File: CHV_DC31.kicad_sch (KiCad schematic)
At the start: 84 parts, among them IC1 W25Q16JVUXIQ_TR, J1 USB_C_Receptacle_USB2.0, J2 Conn_01x02, J3 Conn_02x03_Odd_Even, J4 Conn_02x03_Odd_Even, J5 Conn_02x03_Odd_Even, J6 Conn_01x03, SW2 SW_SPST, SW3 SW_SPST, SW4 SW_SPST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

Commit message: updates
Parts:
- J2: footprint Connector_PinHeader_2.54mm:PinHeader_1x02_P2.54mm_Vertical -> Jumper:SolderJumper-2_P1.3mm_Open_Pad1.0x1.5mm
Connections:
- net RP1_CAN_RX: now also U3.5 (GPIO3); no longer U3.28 (GPIO17)
- net RP1_CAN_TX: now also U3.6 (GPIO4); no longer U3.27 (GPIO16)
- net RP1_LED_1: now also U3.15 (GPIO12); no longer U3.7 (GPIO5)
- net RP1_LED_2: now also U3.16 (GPIO13); no longer U3.8 (GPIO6)
- net RP1_LED_3: now also U3.12 (GPIO9); no longer U3.9 (GPIO7)

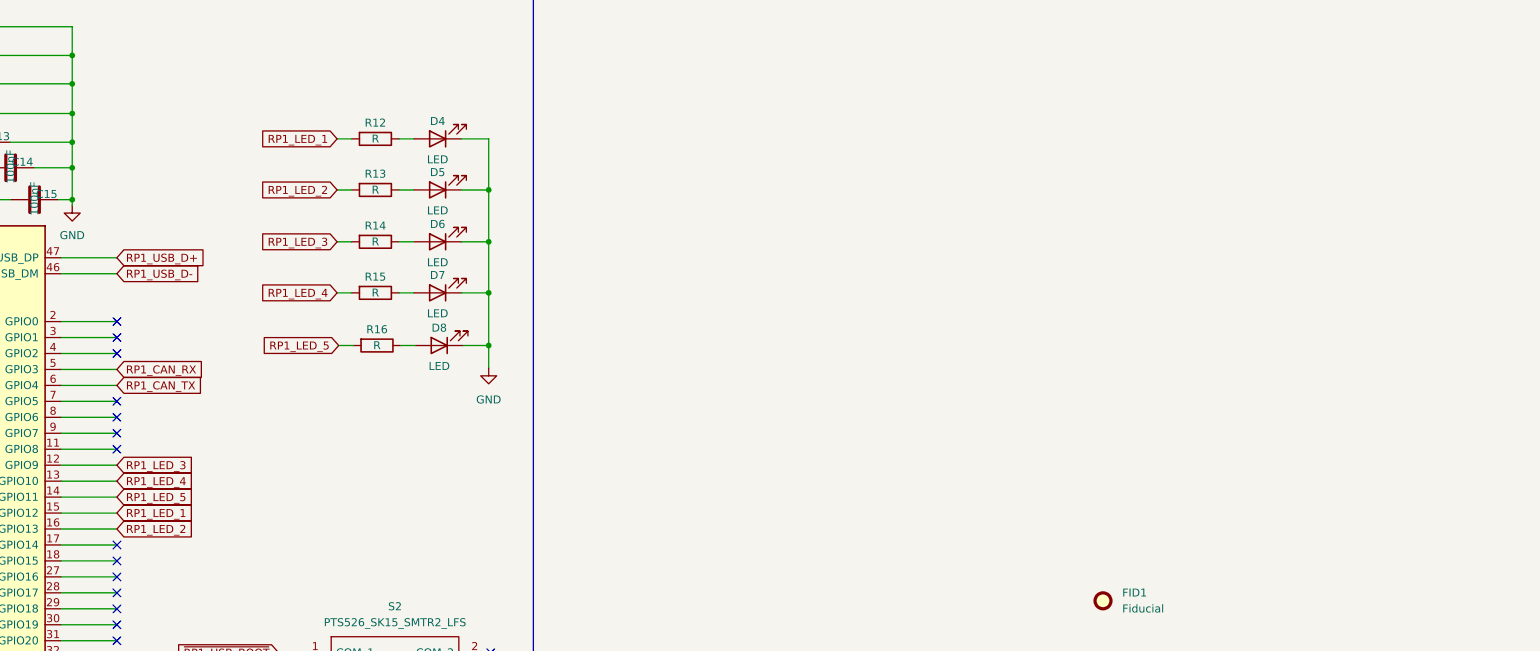
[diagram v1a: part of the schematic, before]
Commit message: layed out led ring
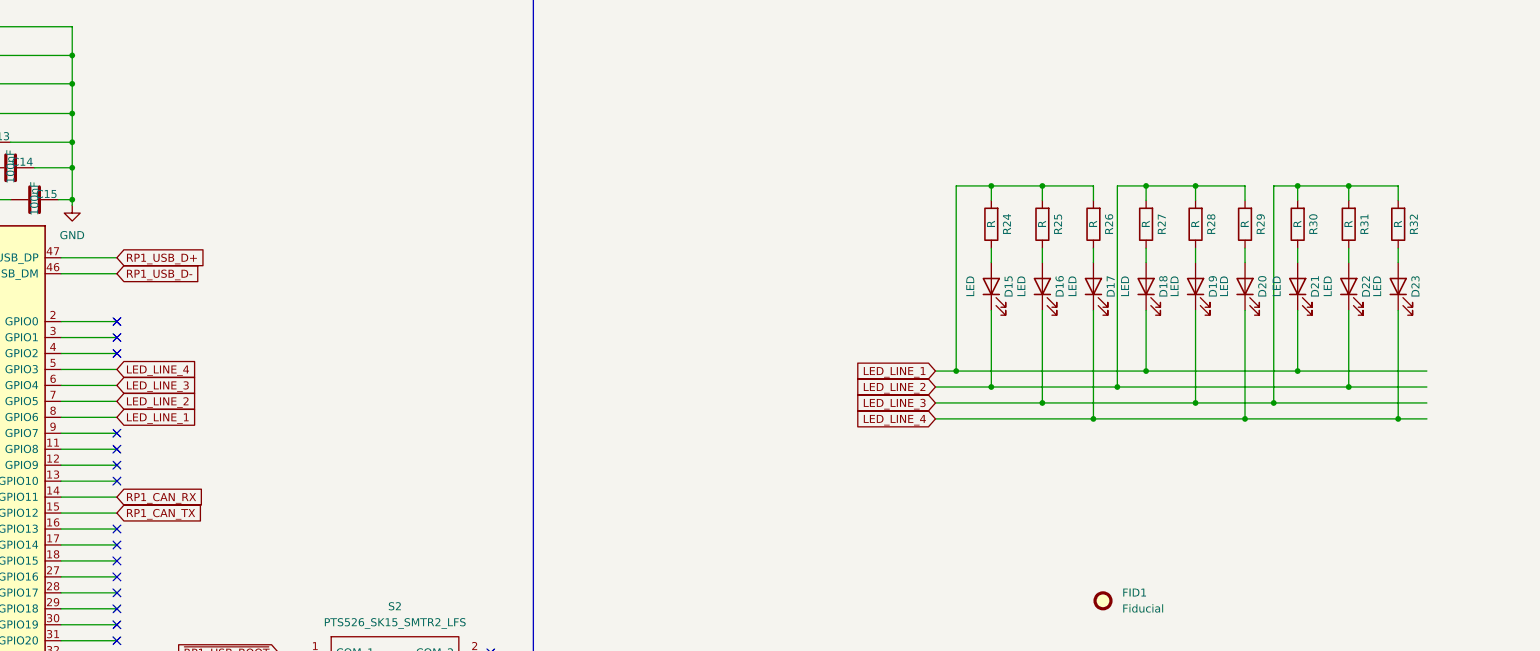
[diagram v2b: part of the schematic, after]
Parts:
- removed D4, D5, D6, D7, D8: LED, LED_SMD:LED_1206_3216Metric, symbol Device:LED
- removed R12, R13, R14, R15, R16: R, Resistor_SMD:R_0805_2012Metric, symbol Device:R
- added D15, D16, D17, D18, D19, D20, D21, D22, D23: LED, LED_SMD:LED_1206_3216Metric, symbol Device:LED
- added R24, R25, R26, R27, R28, R29, R30, R31, R32: R, Resistor_SMD:R_0805_2012Metric, symbol Device:R
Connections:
- net RP1_LED_1 is gone; now on net RP1_CAN_TX: U3.15 (GPIO12)
- net RP1_LED_5 is gone; now on net RP1_CAN_RX: U3.14 (GPIO11)
- net RP1_CAN_RX: no longer U3.5 (GPIO3)
- net RP1_CAN_TX: no longer U3.6 (GPIO4)
- net LED_LINE_2: now reaches U3.7 (GPIO5)
- net LED_LINE_2: now also D15.1 (K), D22.1 (K), R27.2, R28.2, R29.2
- net LED_LINE_1: now reaches U3.8 (GPIO6)
- net LED_LINE_1: now also D18.1 (K), D21.1 (K), R24.2, R25.2, R26.2
- net RP1_LED_2: no longer names the net of U3.16 (GPIO13)
- net RP1_LED_3: no longer names the net of U3.12 (GPIO9)
- net RP1_LED_4: no longer names the net of U3.13 (GPIO10)
- new net: D23.2 (A), R32.1
- new net: D21.2 (A), R30.1
- new net: D19.2 (A), R28.1
- new net: D22.2 (A), R31.1
- new net: D18.2 (A), R27.1
- new net: D16.2 (A), R25.1
- new net: D15.2 (A), R24.1
- new net: D17.2 (A), R26.1
- new net: D20.2 (A), R29.1
- new net LED_LINE_3: D16.1 (K), D19.1 (K), R30.2, R31.2, R32.2, U3.6 (GPIO4)
- new net LED_LINE_4: D17.1 (K), D20.1 (K), D23.1 (K), U3.5 (GPIO3)
- no-connect marks 35 -> 36

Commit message: closer, but also further
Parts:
- removed SW2, SW3, SW4, SW5, SW6, SW7: SW_SPST, OS102011MS2QN1C:OS102011MS2QN1C, symbol Switch:SW_SPST
- added S3, S4, S5, S6, S7, S8: MK-12C02-G020, MK-12C02-G020:MK12C02G020, symbol MK-12C02-G020:MK-12C02-G020
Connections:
- net +3V3: now also S3.2, S4.2, S5.2, S6.2, S7.2
- net GLOBAL_Silent: now also S7.1
- net at J6.3 (Pin_3), R1.2, U1.7 (CANH)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: now also S8.1
- net at R23.2: now also S8.2
- net at D13.1 (K), D14.2 (A), R22.1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: now also S6.1
- net at D2.2 (A), D3.1 (K), R7.1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: now also S3.1
- net at D11.1 (K), D12.2 (A), R20.1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: now also S5.1
- net at D10.2 (A), D9.1 (K), R18.1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: now also S4.1
- no-connect marks 36 -> 66

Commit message: sooooooo close
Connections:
- net +3V3: now also S4.1; no longer S4.2
- net at D13.1 (K), D14.2 (A), R22.1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: now also S6.3; no longer S6.1
- net at D10.2 (A), D9.1 (K), R18.1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: now also S4.2; no longer S4.1
- net at D11.1 (K), D12.2 (A), R20.1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: now also S5.3; no longer S5.1

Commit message: getting closer
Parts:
- added BT1: Battery, symbol Device:Battery
- added C25: 74uF, symbol Device:C
- added C26: 100uF, symbol Device:C
- added D4, D5: D_Schottky, Diode_SMD:D_SOD-123, symbol Device:D_Schottky
- added D6: D_Schottky, symbol Device:D_Schottky
- added L1: 100uH, symbol Device:L
- added Q1: PMOS, symbol Simulation_SPICE:PMOS
- added R12: 100k, symbol Device:R
- added U7: HT75xx-1-SOT89, Package_TO_SOT_SMD:SOT-89-3, symbol Regulator_Linear:HT75xx-1-SOT89
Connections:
- net GND: now also BT1.2 (-), C25.2, C26.2, R12.2, U7.1 (GND)
- net VBUS: now also C26.1, U7.3 (VOUT); no longer C2.1, R9.1, U2.1 (VIN)
- net USB_POWER: now reaches D1.2 (A), J1.A4 (VBUS), J1.A9 (VBUS), J1.B4 (VBUS), J1.B9 (VBUS)
- net USB_POWER: now also D4.2 (A), Q1.2 (G), R12.1
- new net: L1.2, U7.2 (VIN)
- new net: BT1.1 (+), Q1.1 (D)
- new net 3V0 battery: C25.1, D5.2 (A), L1.1, Q1.3 (S)
- new net Common_Power: C2.1, D4.1 (K), D5.1 (K), R9.1, U2.1 (VIN)
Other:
- note added: "TODO: Do I need a diode here??????"
- moved on the sheet: C10, C2, D1, J1, R3, R4, R5, R6, R9, S1, U2

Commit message: more changes
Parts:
- removed D4, D5: D_Schottky, Diode_SMD:D_SOD-123, symbol Device:D_Schottky
- BT1: footprint (none) -> Battery:BatteryHolder_Keystone_2462_2xAA
- C25, C26: footprint (none) -> Capacitor_SMD:C_0805_2012Metric
- D6: footprint (none) -> Diode_SMD:D_SOD-123
- L1: footprint (none) -> Inductor_SMD:L_0805_2012Metric
- Q1: footprint (none) -> Package_TO_SOT_SMD:SOT-23
- R12: footprint (none) -> Resistor_SMD:R_0805_2012Metric
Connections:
- net 3V0 battery is gone; now on net Common_Power: C25.1, L1.1, Q1.3 (S)
- net Common_Power: now also D1.1 (K)
- net USB_POWER: no longer D1.2 (A), J1.A4 (VBUS), J1.A9 (VBUS), J1.B4 (VBUS), J1.B9 (VBUS)
- net VBUS: now also D6.1 (K); no longer D1.1 (K)
- net at L1.2, U7.2 (VIN): now also D6.2 (A)
- new net: D1.2 (A), J1.A4 (VBUS), J1.A9 (VBUS), J1.B4 (VBUS), J1.B9 (VBUS)
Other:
- note removed: "TODO: Do I need a diode here??????"
- moved on the sheet: BT1, C25, C26, D6, L1, Q1, R12, S1, U7

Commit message: getting closer
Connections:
- net +3V3: now also S4.3, S7.3; no longer S4.1, S7.2
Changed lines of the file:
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@@
 (kicad_sch (version 20230121) (generator eeschema)
   (paper "A2")
+  (junction (at 291.338 338.455) (diameter 0) (color 0 0 0 0)
+  )
   (junction (at 254.381 261.874) (diameter 0) (color 255 255 0 1)
   )
@@
   (junction (at 81.026 218.186) (diameter 0) (color 0 0 0 0)
   )
+  (junction (at 276.733 326.771) (diameter 0) (color 0 0 0 0)
+  )
   (junction (at 331.47 76.2) (diameter 0) (color 0 0 0 0)
   )
@@
   (junction (at 395.224 338.074) (diameter 0) (color 0 0 0 0)
   )
-  (junction (at 290.322 338.455) (diameter 0) (color 0 0 0 0)
-  )
   (junction (at 331.47 46.736) (diameter 0) (color 0 0 0 0)
   )
@@
   (junction (at 136.398 30.48) (diameter 0) (color 0 0 0 0)
   )
-  (junction (at 278.257 326.771) (diameter 0) (color 0 0 0 0)
-  )
   (junction (at 89.789 271.526) (diameter 0) (color 0 255 0 1)
   )
@@
   )
   (no_connect (at 463.804 360.68))
-  (no_connect (at 295.402 326.644))
+  (no_connect (at 290.322 326.644))
   (no_connect (at 180.848 325.374))
   (no_connect (at 499.364 300.99))
@@
   (no_connect (at 395.224 300.99))
   (no_connect (at 292.862 301.244))
-  (no_connect (at 180.848 327.914))
+  (no_connect (at 180.848 330.454))
   (no_connect (at 143.51 129.286))
   (no_connect (at 143.51 141.986))
@@
     (stroke (width 0) (type default))
   )
+  (wire (pts (xy 291.338 331.089) (xy 291.338 338.455))
+    (stroke (width 0) (type default))
+  )
   (wire (pts (xy 290.83 66.548) (xy 290.83 81.28))
     (stroke (width 0) (type default))
@@
     (stroke (width 0) (type default))
   )
+  (wire (pts (xy 291.338 338.455) (xy 294.386 338.455))
+    (stroke (width 0) (type default))
+  )
   (wire (pts (xy 41.91 121.666) (xy 45.72 121.666))
     (stroke (width 0) (type default))
   )
-  (wire (pts (xy 184.15 330.454) (xy 184.15 328.93))
+  (wire (pts (xy 184.15 327.914) (xy 184.15 326.39))
     (stroke (width 0) (type default))
   )
@@
     (stroke (width 0) (type default))
   )
-  (wire (pts (xy 278.257 326.771) (xy 268.224 326.771))
-    (stroke (width 0) (type default))
-  )
   (wire (pts (xy 62.23 121.666) (xy 71.12 121.666))
     (stroke (width 0) (type default))
@@
     (stroke (width 0) (type default))
   )
-  (wire (pts (xy 261.747 338.455) (xy 290.322 338.455))
+  (wire (pts (xy 261.747 338.455) (xy 291.338 338.455))
     (stroke (width 0) (type default))
   )
@@
     (stroke (width 0) (type default))
   )
-  (wire (pts (xy 180.848 330.454) (xy 184.15 330.454))
+  (wire (pts (xy 180.848 327.914) (xy 184.15 327.914))
     (stroke (width 0) (type default))
   )
@@
     (stroke (width 0) (type default))
   )
+  (wire (pts (xy 295.402 326.644) (xy 295.402 331.089))
+    (stroke (width 0) (type default))
+  )
   (polyline (pts (xy 473.9894 375.9962) (xy 581.9902 375.9962))
     (stroke (width 0) (type default))
@@
     (stroke (width 0) (type default))
   )
+  (wire (pts (xy 276.733 326.771) (xy 268.224 326.771))
+    (stroke (width 0) (type default))
+  )
   (wire (pts (xy 365.76 335.407) (xy 368.046 335.407))
     (stroke (width 0) (type default))
@@
     (stroke (width 0) (type default))
   )
+  (wire (pts (xy 276.733 326.771) (xy 278.257 326.771))
+    (stroke (width 0) (type default))
+  )
   (wire (pts (xy 339.598 46.736) (xy 347.472 46.736))
     (stroke (width 0) (type default))
@@
     (stroke (width 0) (type default))
   )
-  (wire (pts (xy 290.322 326.644) (xy 290.322 338.455))
-    (stroke (width 0) (type default))
-  )
   (wire (pts (xy 111.76 230.886) (xy 106.68 230.886))
     (stroke (width 0) (type default))
@@
     (stroke (width 0) (type default))
   )
-  (wire (pts (xy 290.322 338.455) (xy 294.386 338.455))
-    (stroke (width 0) (type default))
-  )
   (wire (pts (xy 170.053 187.071) (xy 176.403 187.071))
     (stroke (width 0) (type default))
@@
     (stroke (width 0) (type default))
   )
-  (wire (pts (xy 292.862 326.771) (xy 292.862 326.644))
+  (wire (pts (xy 292.862 328.168) (xy 292.862 326.644))
     (stroke (width 0) (type default))
   )
@@
     (stroke (width 0) (type default))
   )
-  (wire (pts (xy 278.257 326.771) (xy 292.862 326.771))
+  (wire (pts (xy 276.733 328.168) (xy 292.862 328.168))
     (stroke (width 0) (type default))
   )
@@
     (stroke (width 0) (type default))
   )
+  (wire (pts (xy 295.402 331.089) (xy 291.338 331.089))
+    (stroke (width 0) (type default))
+  )
   (wire (pts (xy 537.21 261.874) (xy 537.21 315.214))
     (stroke (width 0) (type default) (color 255 255 0 1))
@@
   )
   (wire (pts (xy 75.2348 30.6324) (xy 68.3768 30.6324))
+    (stroke (width 0) (type default))
+  )
+  (wire (pts (xy 276.733 328.168) (xy 276.733 326.771))
     (stroke (width 0) (type default))
   )
@@
     )
   )
-  (symbol (lib_id "power:+3V3") (at 184.15 328.93 0) (unit 1)
+  (symbol (lib_id "power:+3V3") (at 184.15 326.39 0) (unit 1)
     (in_bom yes) (on_board yes) (dnp no) (fields_autoplaced)
-    (property "Reference" "#PWR027" (at 184.15 332.74 0)
-      (effects (font (size 1.27 1.27)) hide)
-    )
-    (property "Value" "+3V3" (at 184.15 323.469 0)
-      (effects (font (size 1.27 1.27)))
-    )
-    (property "Footprint" "" (at 184.15 328.93 0)
-      (effects (font (size 1.27 1.27)) hide)
-    )
-    (property "Datasheet" "" (at 184.15 328.93 0)
-      (effects (font (size 1.27 1.27)) hide)
-    )
+    (property "Reference" "#PWR027" (at 184.15 330.2 0)
+      (effects (font (size 1.27 1.27)) hide)
+    )
+    (property "Value" "+3V3" (at 184.15 320.929 0)
+      (effects (font (size 1.27 1.27)))
+    )
+    (property "Footprint" "" (at 184.15 326.39 0)
+      (effects (font (size 1.27 1.27)) hide)
+    )
+    (property "Datasheet" "" (at 184.15 326.39 0)
+      (effects (font (size 1.27 1.27)) hide)
+    )

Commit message: almost done!
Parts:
- added R13: R, Resistor_SMD:R_0805_2012Metric, symbol Device:R
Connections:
- net +3V3: now also S3.3; no longer S3.2
- net GND: now also C26.1; no longer C26.2
- net VBUS: now also U7.2 (VOUT), R13.1; no longer C26.1, U7.3 (VOUT)
- net at D6.2 (A), L1.2: now also U7.3 (VIN); no longer U7.2 (VIN)
- net at D2.2 (A), D3.1 (K), R7.1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: now also S3.2; no longer S3.1
- new net: C26.2, R13.2
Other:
- moved on the sheet: C26
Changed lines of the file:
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@@
   (junction (at 472.186 326.39) (diameter 0) (color 0 0 0 0)
   )
+  (junction (at 56.388 206.502) (diameter 0) (color 0 0 0 0)
+  )
   (junction (at 364.109 338.074) (diameter 0) (color 0 0 0 0)
   )
@@
   (junction (at 259.461 271.526) (diameter 0) (color 0 255 0 1)
   )
-  (junction (at 56.388 206.502) (diameter 0) (color 0 0 0 0)
-  )
   (junction (at 242.57 314.071) (diameter 0) (color 0 0 0 0)
   )
@@
   (junction (at 193.802 381.508) (diameter 0) (color 0 0 0 0)
   )
-  (junction (at 70.993 218.186) (diameter 0) (color 0 0 0 0)
-  )
   (junction (at 123.952 348.615) (diameter 0) (color 0 0 0 0)
   )
@@
   (junction (at 539.75 271.526) (diameter 0) (color 0 255 0 1)
   )
+  (junction (at 70.993 218.186) (diameter 0) (color 0 0 0 0)
+  )
   (junction (at 172.974 148.336) (diameter 0) (color 0 0 0 0)
   )
@@
   (no_connect (at 51.308 218.186))
   (no_connect (at 143.51 126.746))
-  (no_connect (at 53.848 218.186))
+  (no_connect (at 58.928 218.186))
   (no_connect (at 155.448 330.454))
   (no_connect (at 155.448 332.994))
@@
     (stroke (width 0) (type default))
   )
+  (wire (pts (xy 53.848 218.186) (xy 53.848 206.502))
+    (stroke (width 0) (type default))
+  )
   (wire (pts (xy 169.2402 121.031) (xy 172.5422 121.031))
     (stroke (width 0) (type default))
@@
     (stroke (width 0) (type default))
   )
+  (wire (pts (xy 126.238 360.807) (xy 126.365 360.807))
+    (stroke (width 0) (type default))
+  )
   (wire (pts (xy 565.912 244.221) (xy 565.912 249.301))
     (stroke (width 0) (type default))
@@
     (stroke (width 0) (type default))
   )
+  (wire (pts (xy 53.848 206.502) (xy 56.388 206.502))
+    (stroke (width 0) (type default))
+  )
   (wire (pts (xy 178.054 153.416) (xy 178.054 160.909))
     (stroke (width 0) (type default))
@@
     (stroke (width 0) (type default))
   )
+  (wire (pts (xy 56.388 218.186) (xy 56.388 217.043))
+    (stroke (width 0) (type default))
+  )
   (wire (pts (xy 347.472 56.642) (xy 347.472 58.928))
     (stroke (width 0) (type default))
@@
     (stroke (width 0) (type default))
   )
+  (wire (pts (xy 114.808 360.807) (xy 118.618 360.807))
+    (stroke (width 0) (type default))
+  )
   (wire (pts (xy 136.398 39.7764) (xy 136.398 43.8404))
     (stroke (width 0) (type default))
@@
     (stroke (width 0) (type default))
   )
-  (wire (pts (xy 58.928 218.186) (xy 70.993 218.186))
-    (stroke (width 0) (type default))
-  )
   (wire (pts (xy 361.823 271.526) (xy 463.423 271.526))
     (stroke (width 0) (type default) (color 0 255 0 1))
@@
     (stroke (width 0) (type default))
   )
-  (wire (pts (xy 126.365 348.615) (xy 126.365 353.187))
+  (wire (pts (xy 126.365 348.615) (xy 126.365 351.028))
     (stroke (width 0) (type default))
   )
@@
     (stroke (width 0) (type default))
   )
+  (wire (pts (xy 70.993 217.043) (xy 70.993 218.186))
+    (stroke (width 0) (type default))
+  )
   (wire (pts (xy 113.2332 35.2044) (xy 109.22 35.2044))
     (stroke (width 0) (type default))
@@
     (stroke (width 0) (type default))
   )
+  (wire (pts (xy 56.388 217.043) (xy 70.993 217.043))
+    (stroke (width 0) (type default))
+  )
   (wire (pts (xy 365.76 334.01) (xy 365.76 335.407))
     (stroke (width 0) (type default))
@@
     (stroke (width 0) (type default))
   )
-  (wire (pts (xy 56.388 218.186) (xy 56.388 206.502))
-    (stroke (width 0) (type default))
-  )
   (wire (pts (xy 136.398 43.8404) (xy 136.398 48.9204))
     (stroke (width 0) (type default))
@@
     (stroke (width 0) (type default))
   )
+  (wire (pts (xy 126.365 358.648) (xy 126.365 360.807))
+    (stroke (width 0) (type default))
+  )
   (wire (pts (xy 104.14 50.546) (xy 104.14 25.9588))
     (stroke (width 0) (type default))
@@
     (stroke (width 0) (type default))
   )
-  (wire (pts (xy 114.808 360.807) (xy 126.365 360.807))
-    (stroke (width 0) (type default))
-  )
   (wire (pts (xy 395.224 326.39) (xy 395.224 338.074))
     (stroke (width 0) (type default))
@@
       (effects (font (size 1.27 1.27) italic) hide)
     )
-    (property "Datasheet" "https://www.holtek.com/documents/10179/116711/HT75xx-1v250.pdf" (at 114.808 348.615 0)
+    (property "Datasheet" "https://www.holtek.com/documents/10179/116711/HT75xx-1v250.pdf" (at 121.158 360.045 0)
       (effects (font (size 1.27 1.27)) hide)
     )
     (pin "1")
-    (pin "2")
     (pin "3")
+    (pin "2")
     (instances
       (project "CHV_DC31"
@@
     )
   )
-  (symbol (lib_id "Device:C") (at 126.365 356.997 0) (unit 1)
+  (symbol (lib_id "Device:C") (at 122.428 360.807 90) (unit 1)
     (in_bom yes) (on_board yes) (dnp no) (fields_autoplaced)
-    (property "Reference" "C26" (at 129.413 356.362 0)
-      (effects (font (size 1.27 1.27)) (justify left))
+    (property "Reference" "C26" (at 122.428 354.965 90)
+      (effects (font (size 1.27 1.27)))
     )
-    (property "Value" "100uF" (at 129.413 358.902 0)
-      (effects (font (size 1.27 1.27)) (justify left))
+    (property "Value" "100uF" (at 122.428 357.505 90)
+      (effects (font (size 1.27 1.27)))
     )
-    (property "Footprint" "Capacitor_SMD:C_0805_2012Metric" (at 127.3302 360.807 0)
+    (property "Footprint" "Capacitor_SMD:C_0805_2012Metric" (at 126.238 359.8418 0)
       (effects (font (size 1.27 1.27)) hide)
     )
-    (property "Datasheet" "~" (at 126.365 356.997 0)
+    (property "Datasheet" "~" (at 122.428 360.807 0)
       (effects (font (size 1.27 1.27)) hide)
     )
@@
         )
       )
+    )
+  )
+  (symbol (lib_id "Device:R") (at 126.365 354.838 0) (unit 1)
+    (in_bom yes) (on_board yes) (dnp no) (fields_autoplaced)
+    (property "Reference" "R13" (at 129.286 354.203 0)
+      (effects (font (size 1.27 1.27)) (justify left))
+    )
+    (property "Value" "R" (at 129.286 356.743 0)
+      (effects (font (size 1.27 1.27)) (justify left))
+    )
+    (property "Footprint" "Resistor_SMD:R_0805_2012Metric" (at 124.587 354.838 90)
+      (effects (font (size 1.27 1.27)) hide)
+    )
+    (property "Datasheet" "~" (at 126.365 354.838 0)
+      (effects (font (size 1.27 1.27)) hide)
+    )
+    (pin "1")
+    (pin "2")
+    (instances
+      (project "CHV_DC31"
+        (path "/8c2b2004-cf2c-4944-a323-f4295d94980b"
+          (reference "R13") (unit 1)
+        )
+      )
